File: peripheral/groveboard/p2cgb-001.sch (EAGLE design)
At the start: 8 parts

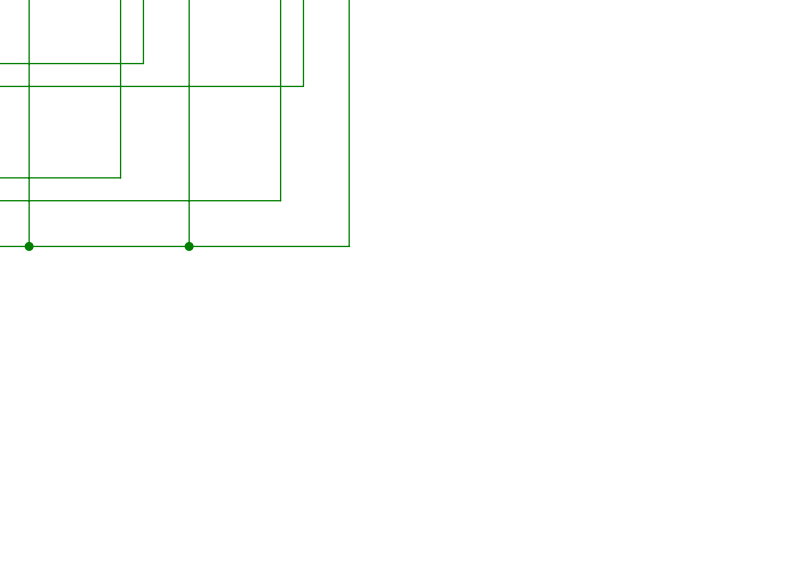
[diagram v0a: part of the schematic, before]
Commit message: Added bogopins to connect the logicboard and the groveboard.
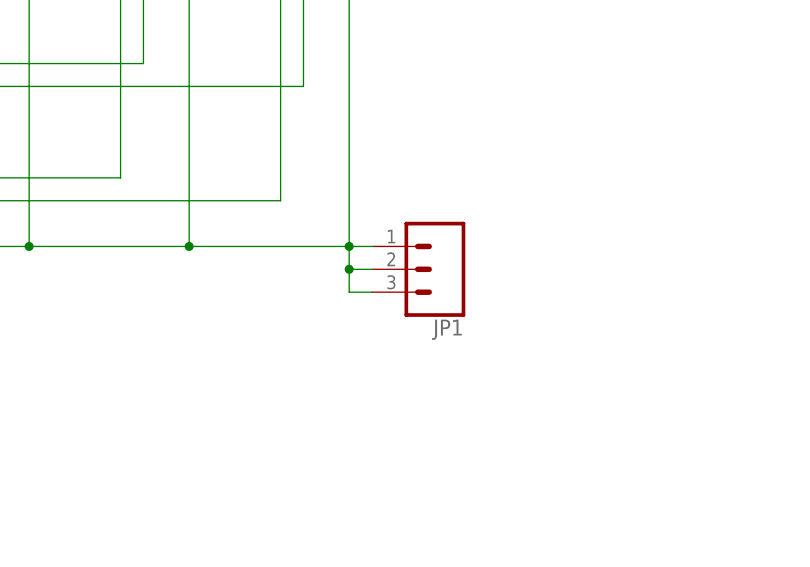
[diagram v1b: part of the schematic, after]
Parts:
- added JP1: (no value), SparkFun-Connectors:CONN_03
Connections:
- net GND: now also JP1.1, JP1.2, JP1.3
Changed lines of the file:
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@@
 <part name="J3" library="SparkFun-Connectors" library_urn="urn:adsk.eagle:library:513" deviceset="CONN_04" device="JST-PTH" package3d_urn="urn:adsk.eagle:package:38101/1"/>
 <part name="J4" library="SparkFun-Connectors" library_urn="urn:adsk.eagle:library:513" deviceset="CONN_04" device="JST-PTH" package3d_urn="urn:adsk.eagle:package:38101/1"/>
+<part name="JP1" library="SparkFun-Connectors" library_urn="urn:adsk.eagle:library:513" deviceset="CONN_03" device="" package3d_urn="urn:adsk.eagle:package:38063/1"/>
 </parts>
 <sheets>
@@
 <attribute name="NAME" x="147.828" y="137.16" size="1.778" layer="95" font="vector" rot="R270"/>
 </instance>
+<instance part="JP1" gate="J$1" x="154.94" y="81.28" smashed="yes" rot="R180">
+<attribute name="VALUE" x="157.48" y="88.646" size="1.778" layer="96" font="vector" rot="R180"/>
+<attribute name="NAME" x="157.48" y="75.692" size="1.778" layer="95" font="vector" rot="R180"/>
+</instance>
 </instances>
 <busses>
@@
 <wire x1="144.78" y1="83.82" x2="144.78" y2="127" width="0.1524" layer="91"/>
 <junction x="127" y="83.82"/>
+<pinref part="JP1" gate="J$1" pin="1"/>
+<wire x1="144.78" y1="83.82" x2="147.32" y2="83.82" width="0.1524" layer="91"/>
+<junction x="144.78" y="83.82"/>
+<pinref part="JP1" gate="J$1" pin="2"/>
+<wire x1="147.32" y1="81.28" x2="144.78" y2="81.28" width="0.1524" layer="91"/>
+<wire x1="144.78" y1="81.28" x2="144.78" y2="83.82" width="0.1524" layer="91"/>
+<pinref part="JP1" gate="J$1" pin="3"/>
+<wire x1="147.32" y1="78.74" x2="144.78" y2="78.74" width="0.1524" layer="91"/>
+<wire x1="144.78" y1="78.74" x2="144.78" y2="81.28" width="0.1524" layer="91"/>
+<junction x="144.78" y="81.28"/>
 </segment>
 </net>
